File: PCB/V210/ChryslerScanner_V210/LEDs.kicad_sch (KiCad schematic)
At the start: 16 parts, among them Q2 AO3400A, Q3 AO3400A, Q4 AO3400A, Q5 AO3400A

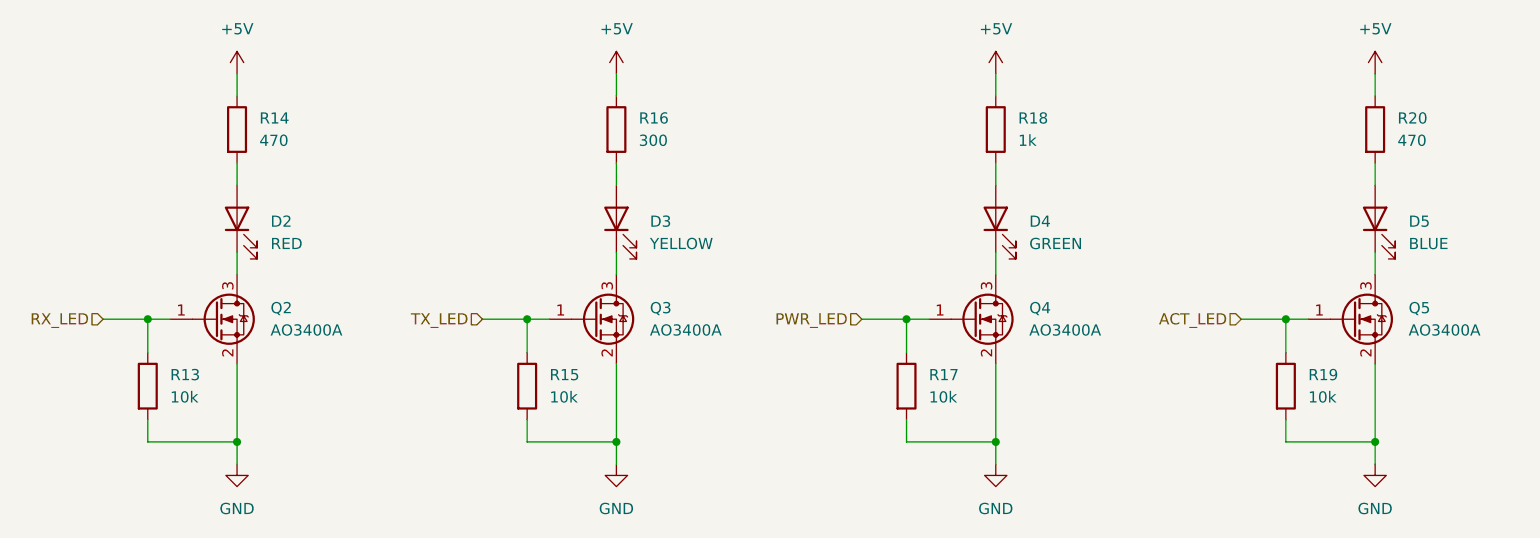
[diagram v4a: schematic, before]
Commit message: Added CCD back in - needed for early TJs.
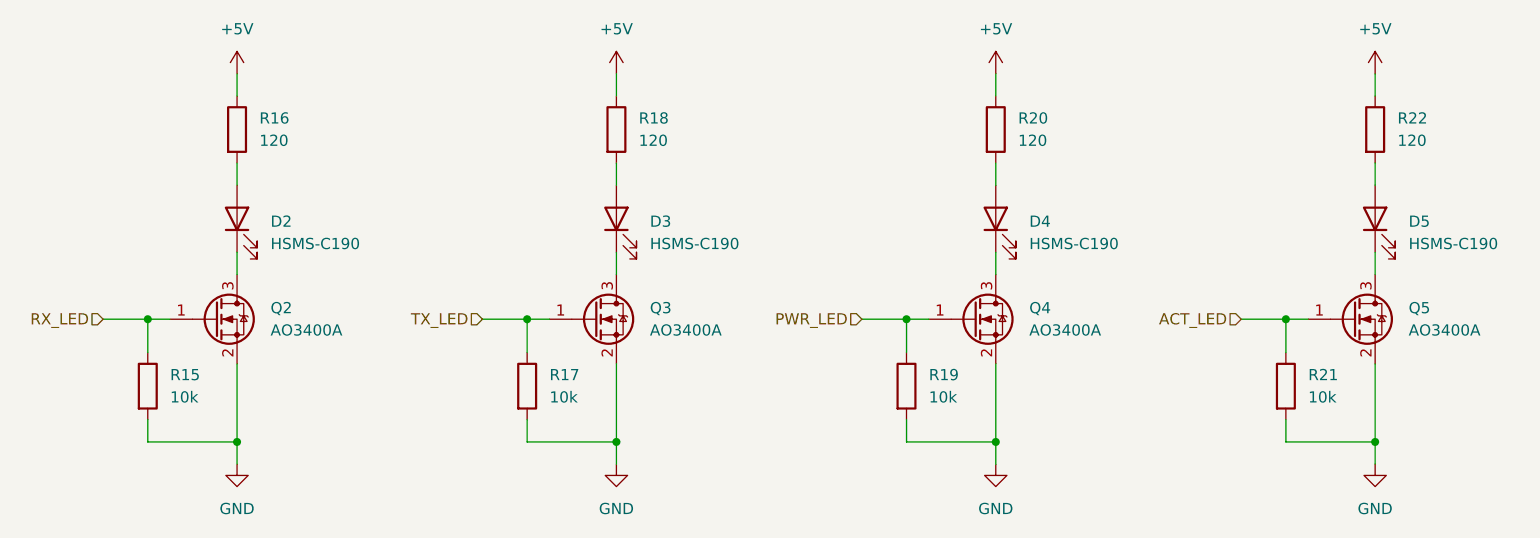
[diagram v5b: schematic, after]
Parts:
- D2: value RED -> HSMS-C190; footprint (none) -> LED_SMD:LED_0603_1608Metric
- D3: value YELLOW -> HSMS-C190; footprint (none) -> LED_SMD:LED_0603_1608Metric
- D4: value GREEN -> HSMS-C190; footprint (none) -> LED_SMD:LED_0603_1608Metric
- D5: value BLUE -> HSMS-C190; footprint (none) -> LED_SMD:LED_0603_1608Metric
- R16: renamed from R14; value 470 -> 120
- R18: renamed from R16; value 300 -> 120
- R20: renamed from R18; value 1k -> 120
- R22: renamed from R20; value 470 -> 120
- renumbered R13 to R15, R15 to R17, R17 to R19, R19 to R21
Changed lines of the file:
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@@
   (title_block
     (title "TJ Diag")
-    (date "2023-07-06")
+    (date "2023-07-07")
     (rev "V1.00")
     (company "andy@britishideas.com")
@@
   (symbol (lib_id "Device:R") (at 74.93 110.49 0) (unit 1)
     (in_bom yes) (on_board yes) (fields_autoplaced)
-    (property "Reference" "R13" (id 0) (at 77.47 109.2199 0)
+    (property "Reference" "R15" (id 0) (at 77.47 109.2199 0)
       (effects (font (size 1.27 1.27)) (justify left))
     )
@@
       (effects (font (size 1.27 1.27)) (justify right))
     )
-    (property "Value" "RED" (id 1) (at 88.9 94.2974 90)
-      (effects (font (size 1.27 1.27)) (justify right))
-    )
-    (property "Footprint" "" (id 2) (at 85.09 91.44 0)
+    (property "Value" "HSMS-C190" (id 1) (at 88.9 94.2974 90)
+      (effects (font (size 1.27 1.27)) (justify right))
+    )
+    (property "Footprint" "LED_SMD:LED_0603_1608Metric" (id 2) (at 85.09 91.44 0)
       (effects (font (size 1.27 1.27)) hide)
     )
@@
   (symbol (lib_id "Device:R") (at 161.29 110.49 0) (unit 1)
     (in_bom yes) (on_board yes) (fields_autoplaced)
-    (property "Reference" "R17" (id 0) (at 163.83 109.2199 0)
+    (property "Reference" "R19" (id 0) (at 163.83 109.2199 0)
       (effects (font (size 1.27 1.27)) (justify left))
     )
@@
   (symbol (lib_id "Device:R") (at 85.09 81.28 0) (unit 1)
     (in_bom yes) (on_board yes) (fields_autoplaced)
-    (property "Reference" "R14" (id 0) (at 87.63 80.0099 0)
-      (effects (font (size 1.27 1.27)) (justify left))
-    )
-    (property "Value" "470" (id 1) (at 87.63 82.5499 0)
+    (property "Reference" "R16" (id 0) (at 87.63 80.0099 0)
+      (effects (font (size 1.27 1.27)) (justify left))
+    )
+    (property "Value" "120" (id 1) (at 87.63 82.5499 0)
       (effects (font (size 1.27 1.27)) (justify left))
     )
@@
   (symbol (lib_id "Device:R") (at 214.63 81.28 0) (unit 1)
     (in_bom yes) (on_board yes) (fields_autoplaced)
-    (property "Reference" "R20" (id 0) (at 217.17 80.0099 0)
-      (effects (font (size 1.27 1.27)) (justify left))
-    )
-    (property "Value" "470" (id 1) (at 217.17 82.5499 0)
+    (property "Reference" "R22" (id 0) (at 217.17 80.0099 0)
+      (effects (font (size 1.27 1.27)) (justify left))
+    )
+    (property "Value" "120" (id 1) (at 217.17 82.5499 0)
       (effects (font (size 1.27 1.27)) (justify left))
     )
@@
   (symbol (lib_id "Device:R") (at 171.45 81.28 0) (unit 1)
     (in_bom yes) (on_board yes) (fields_autoplaced)
-    (property "Reference" "R18" (id 0) (at 173.99 80.0099 0)
-      (effects (font (size 1.27 1.27)) (justify left))
-    )
-    (property "Value" "1k" (id 1) (at 173.99 82.5499 0)
+    (property "Reference" "R20" (id 0) (at 173.99 80.0099 0)
+      (effects (font (size 1.27 1.27)) (justify left))
+    )
+    (property "Value" "120" (id 1) (at 173.99 82.5499 0)
       (effects (font (size 1.27 1.27)) (justify left))
     )
@@
   (symbol (lib_id "Device:R") (at 118.11 110.49 0) (unit 1)
     (in_bom yes) (on_board yes) (fields_autoplaced)
-    (property "Reference" "R15" (id 0) (at 120.65 109.2199 0)
+    (property "Reference" "R17" (id 0) (at 120.65 109.2199 0)
       (effects (font (size 1.27 1.27)) (justify left))
     )
@@
       (effects (font (size 1.27 1.27)) (justify right))
     )
-    (property "Value" "YELLOW" (id 1) (at 132.08 94.2974 90)
-      (effects (font (size 1.27 1.27)) (justify right))
-    )
-    (property "Footprint" "" (id 2) (at 128.27 91.44 0)
+    (property "Value" "HSMS-C190" (id 1) (at 132.08 94.2974 90)
+      (effects (font (size 1.27 1.27)) (justify right))
+    )
+    (property "Footprint" "LED_SMD:LED_0603_1608Metric" (id 2) (at 128.27 91.44 0)
       (effects (font (size 1.27 1.27)) hide)
     )
@@
       (effects (font (size 1.27 1.27)) (justify right))
     )
-    (property "Value" "GREEN" (id 1) (at 175.26 94.2974 90)
-      (effects (font (size 1.27 1.27)) (justify right))
-    )
-    (property "Footprint" "" (id 2) (at 171.45 91.44 0)
+    (property "Value" "HSMS-C190" (id 1) (at 175.26 94.2974 90)
+      (effects (font (size 1.27 1.27)) (justify right))
+    )
+    (property "Footprint" "LED_SMD:LED_0603_1608Metric" (id 2) (at 171.45 91.44 0)
       (effects (font (size 1.27 1.27)) hide)
     )
@@
   (symbol (lib_id "Device:R") (at 204.47 110.49 0) (unit 1)
     (in_bom yes) (on_board yes) (fields_autoplaced)
-    (property "Reference" "R19" (id 0) (at 207.01 109.2199 0)
+    (property "Reference" "R21" (id 0) (at 207.01 109.2199 0)
       (effects (font (size 1.27 1.27)) (justify left))
     )
@@
       (effects (font (size 1.27 1.27)) (justify right))
     )
-    (property "Value" "BLUE" (id 1) (at 218.44 94.2974 90)
-      (effects (font (size 1.27 1.27)) (justify right))
-    )
-    (property "Footprint" "" (id 2) (at 214.63 91.44 0)
+    (property "Value" "HSMS-C190" (id 1) (at 218.44 94.2974 90)
+      (effects (font (size 1.27 1.27)) (justify right))
+    )
+    (property "Footprint" "LED_SMD:LED_0603_1608Metric" (id 2) (at 214.63 91.44 0)
       (effects (font (size 1.27 1.27)) hide)
     )
@@
   (symbol (lib_id "Device:R") (at 128.27 81.28 0) (unit 1)
     (in_bom yes) (on_board yes) (fields_autoplaced)
-    (property "Reference" "R16" (id 0) (at 130.81 80.0099 0)
-      (effects (font (size 1.27 1.27)) (justify left))
-    )
-    (property "Value" "300" (id 1) (at 130.81 82.5499 0)
-      (effects (font (size 1.27 1.27)) (justify left))
-    )
+    (property "Reference" "R18" (id 0) (at 130.81 80.0099 0)
+      (effects (font (size 1.27 1.27)) (justify left))
+    )
+    (property "Value" "120" (id 1) (at 130.81 82.5499 0)
+      (effects (font (size 1.27 1.27)) (justify left))
+    )
